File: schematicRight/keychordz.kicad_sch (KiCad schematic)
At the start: 41 parts, among them IC1 MCP73833-BZI_UN, J1 USB_C_Receptacle_USB2.0, J2 Conn_01x04_Male, J3 Conn_01x04_Male, SW1 SW_Push, SW2 SW_Push, SW3 SW_Push, SW4 SW_Push, SW5 SW_Push, SW6 SW_Push, SW7 SW_Push, SW9 SW_SPST, U1 nRF52840_Breakout

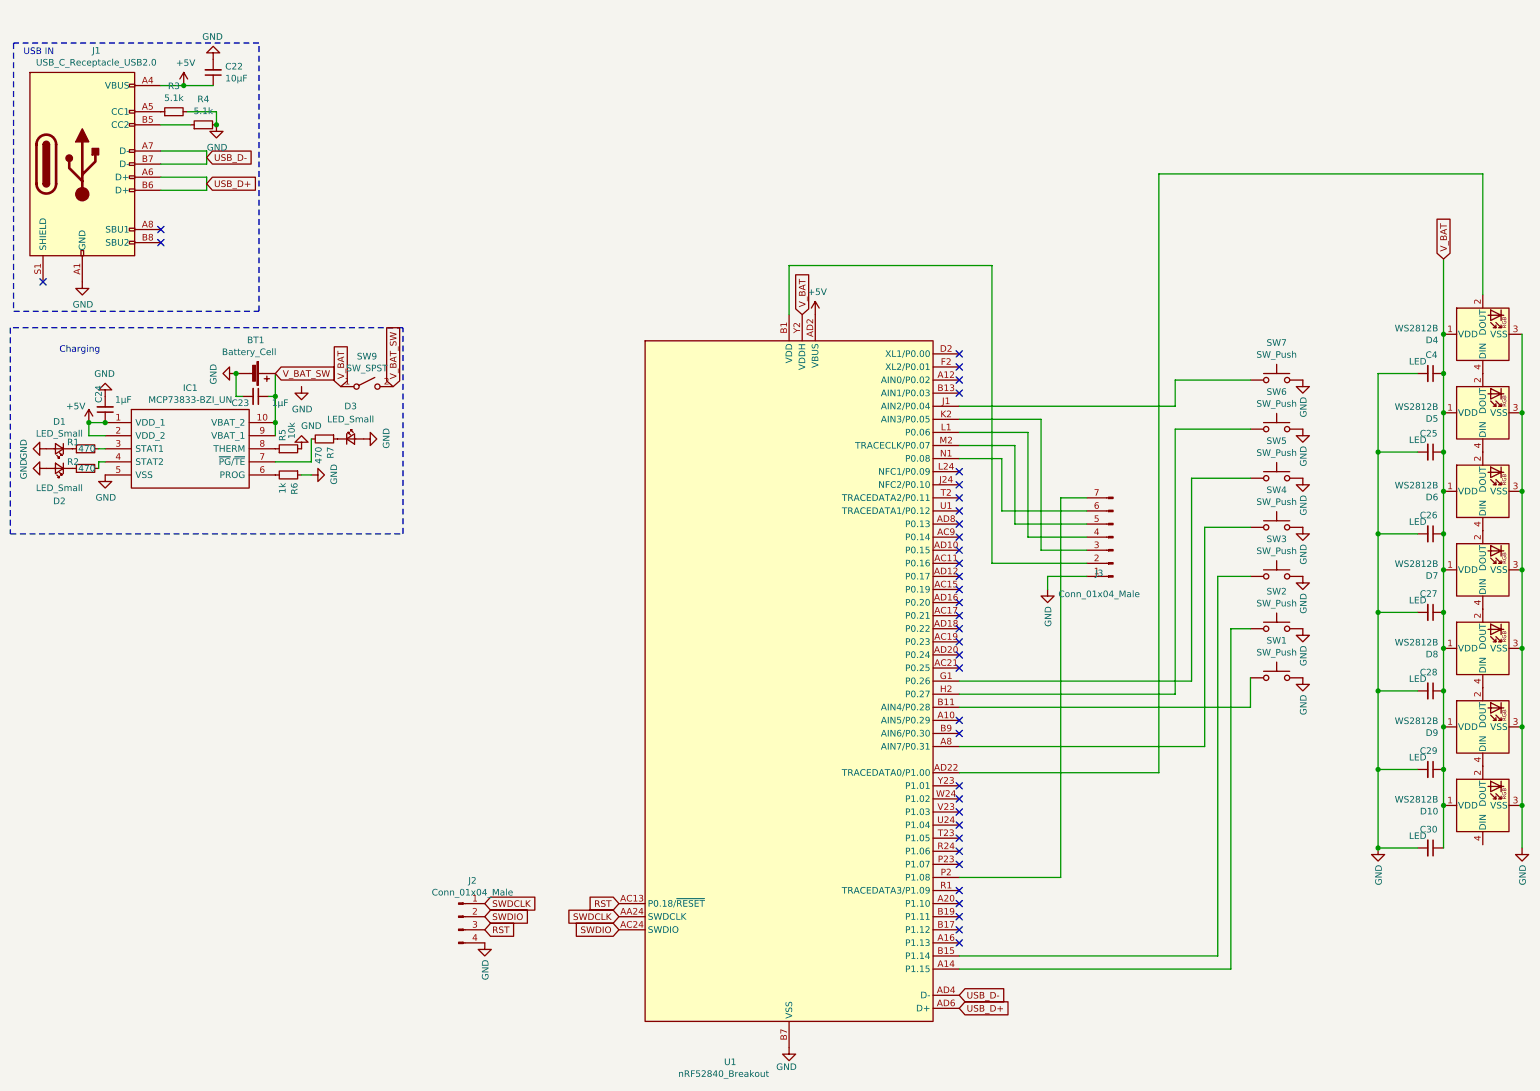
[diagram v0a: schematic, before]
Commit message: change right PCB to STM32
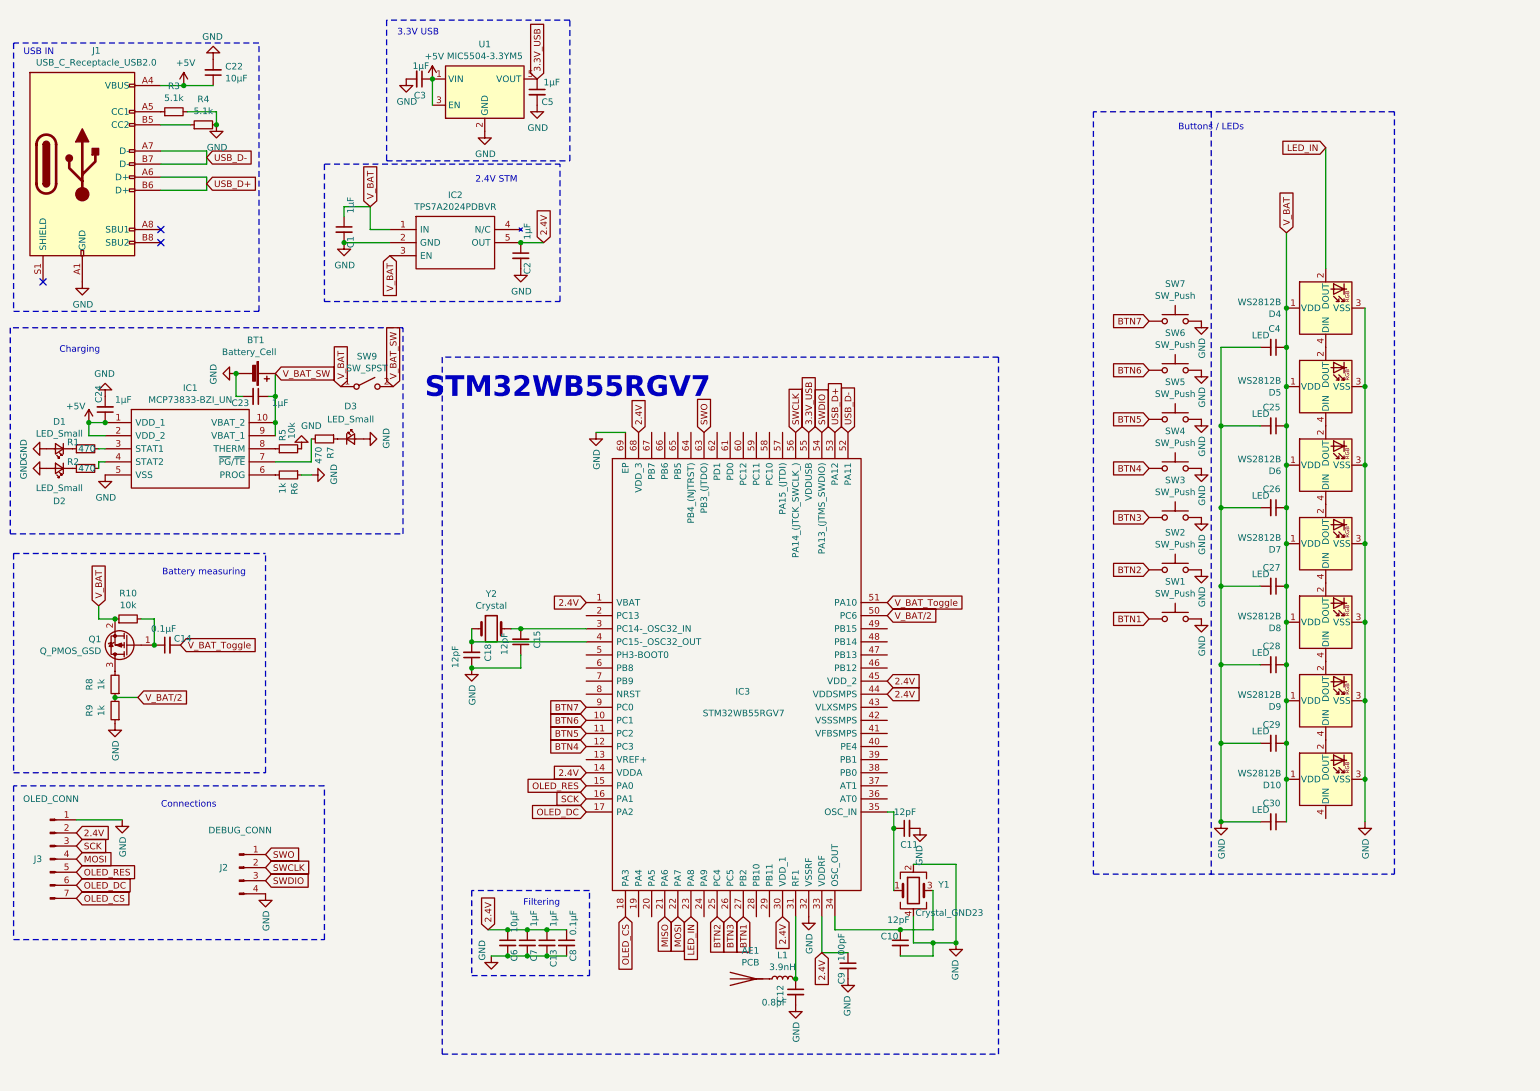
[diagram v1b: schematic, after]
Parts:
- removed U1: nRF52840_Breakout, schematic:nRF52840_Breakout, symbol MCU_Nordic:nRF52840_Breakout
- added AE1: PCB, RF_Antenna:Texas_SWRA117D_2.4GHz_Left, symbol Device:Antenna
- added C1, C13, C2, C3, C5, C7: 1µF, Capacitor_SMD:C_0402_1005Metric_Pad0.74x0.62mm_HandSolder, symbol Device:C_Small
- added C10, C11, C15, C18: 12pF, Capacitor_SMD:C_0603_1608Metric_Pad1.08x0.95mm_HandSolder, symbol Device:C_Small
- added C12: 0.8pF, Capacitor_SMD:C_0201_0603Metric_Pad0.64x0.40mm_HandSolder, symbol Device:C_Small
- added C14, C8: 0.1µF, Capacitor_SMD:C_0402_1005Metric_Pad0.74x0.62mm_HandSolder, symbol Device:C_Small
- added C6: 10µF, Capacitor_SMD:C_0402_1005Metric_Pad0.74x0.62mm_HandSolder, symbol Device:C_Small
- added C9: 100pF, Capacitor_SMD:C_0402_1005Metric_Pad0.74x0.62mm_HandSolder, symbol Device:C_Small
- added IC2: TPS7A2024PDBVR, SamacSys_Parts:SOT95P280X145-5N, symbol LoaderParts:TPS7A2033PDBVR
- added IC3: STM32WB55RGV7, SamacSys_Parts:QFN40P800X800X100-69N-D, symbol LoaderParts:STM32WB55RGV7
- added L1: 3.9nH, Inductor_SMD:L_0402_1005Metric_Pad0.77x0.64mm_HandSolder, symbol Device:L_Small
- added Q1: Q_PMOS_GSD, Package_TO_SOT_SMD:SC-59_Handsoldering, symbol Device:Q_PMOS_GSD
- added R10: 10k, Resistor_SMD:R_0603_1608Metric_Pad0.98x0.95mm_HandSolder, symbol Device:R_Small
- added R8, R9: 1k, Resistor_SMD:R_0603_1608Metric_Pad0.98x0.95mm_HandSolder, symbol Device:R_Small
- added U1: MIC5504-3.3YM5, Package_TO_SOT_SMD:SOT-23-5, symbol Regulator_Linear:MIC5504-3.3YM5
- added Y1: Crystal_GND23, Crystal:Crystal_SMD_2016-4Pin_2.0x1.6mm_HandSoldering, symbol Device:Crystal_GND24
- added Y2: Crystal, Crystal:Crystal_SMD_MicroCrystal_CC7V-T1A-2Pin_3.2x1.5mm_HandSoldering, symbol Device:Crystal
- J1: footprint Connector_USB:USB_C_Receptacle_Amphenol_12401548E4-2A -> SamacSys_Parts:SS52400002
- J2: value Conn_01x04_Male -> DEBUG_CONN
- J3: value Conn_01x04_Male -> OLED_CONN
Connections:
- net RST is gone; now on net SWDIO: J2.3 (Pin_3)
- net +5V: now also C3.1, U1.1 (VIN), U1.3 (EN)
- net GND: now also C1.2, C10.2, C11.2, C12.2, C13.2, C15.1, C18.1, C2.2, C3.2, C5.2, C6.2, C7.2, C8.2, C9.2, IC2.2 (GND), IC3.32 (VSSRF), IC3.69 (EP), R9.1, U1.2 (GND), Y1.2, Y1.4
- net SWDIO: now also IC3.54 (PA13_(JTMS_SWDIO)); no longer J2.2 (Pin_2)
- net USB_D+: now also IC3.53 (PA12)
- net USB_D-: now also IC3.52 (PA11)
- net V_BAT: now also C1.1, IC2.1 (IN), IC2.3 (EN), Q1.2 (S), R10.1
- net BTN5: now reaches SW5.1
- net BTN5: now also IC3.11 (PC2)
- net BTN4: now reaches SW4.1
- net BTN4: now also IC3.12 (PC3)
- net BTN3: now reaches SW3.1
- net BTN3: now also IC3.26 (PC5)
- net BTN2: now reaches SW2.1
- net BTN2: now also IC3.25 (PC4)
- net BTN1: now reaches SW1.1
- net BTN1: now also IC3.27 (PB2)
- net 2.4V: now reaches J3.2 (Pin_2)
- net 2.4V: now also C13.1, C2.1, C6.1, C7.1, C8.1, C9.1, IC2.5 (OUT), IC3.1 (VBAT), IC3.14 (VDDA), IC3.30 (VDD_1), IC3.33 (VDDRF), IC3.44 (VDDSMPS), IC3.45 (VDD_2), IC3.68 (VDD_3)
- net SCK: now reaches J3.3 (Pin_3)
- net SCK: now also IC3.16 (PA1)
- net MOSI: now reaches J3.4 (Pin_4)
- net MOSI: now also IC3.22 (PA7)
- net OLED_RES: now reaches J3.5 (Pin_5)
- net OLED_RES: now also IC3.15 (PA0)
- net OLED_DC: now reaches J3.6 (Pin_6)
- net OLED_DC: now also IC3.17 (PA2)
- net OLED_CS: now reaches J3.7 (Pin_7)
- net OLED_CS: now also IC3.18 (PA3)
- net BTN6: now reaches SW6.1
- net BTN6: now also IC3.10 (PC1)
- net LED_IN: now reaches D4.2 (DOUT)
- net LED_IN: now also IC3.23 (PA8)
- net BTN7: now reaches SW7.1
- net BTN7: now also IC3.9 (PC0)
- net SWDCLK renamed SWO
- net SWO: now also IC3.63 (PB3_(JTDO))
- new net: C12.1, IC3.31 (RF1), L1.2
- new net: C14.1, Q1.1 (G), R10.2
- new net: C15.2, IC3.3 (PC14-_OSC32_IN), Y2.2
- new net: C10.1, IC3.34 (OSC_OUT), Y1.3
- new net: C11.1, IC3.35 (OSC_IN), Y1.1
- new net: C18.2, IC3.4 (PC15-_OSC32_OUT), Y2.1
- new net: Q1.3 (D), R8.2
- new net: AE1.1 (A), L1.1
- new net 3.3V_USB: C5.1, IC3.55 (VDDUSB), U1.5 (VOUT)
- new net MISO: IC3.21 (PA6)
- new net SWCLK: IC3.56 (PA14_(JTCK_SWCLK_)), J2.2 (Pin_2)
- new net V_BAT_Toggle: C14.2, IC3.51 (PA10)
- new net V_BAT/2: IC3.50 (PC6), R8.1, R9.2
- no-connect marks 37 -> 3
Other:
- note added: "2.4V STM"
- note added: "3.3V USB"
- note added: "Battery measuring"
- note added: "Buttons / LEDs"
- note added: "Connections"
- note added: "Filtering"
- note added: "STM32WB55RGV7"
- moved on the sheet: C25, C26, C27, C28, C29, C30, C4, D10, D4, D5, D6, D7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

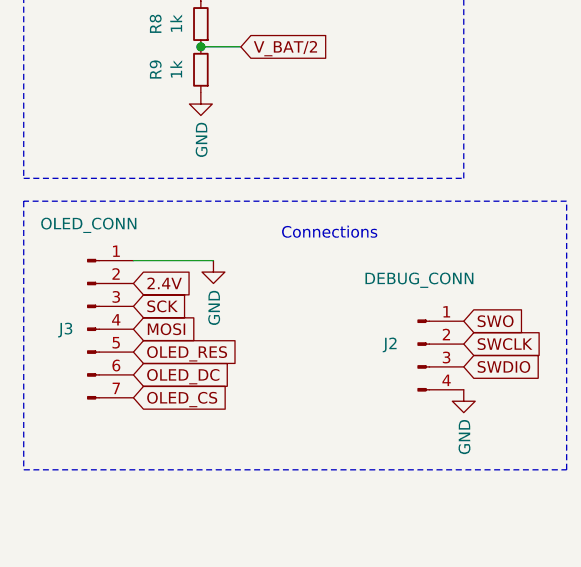
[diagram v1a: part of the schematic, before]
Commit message: change OLED voltage to V_BAT (ordered this commit)
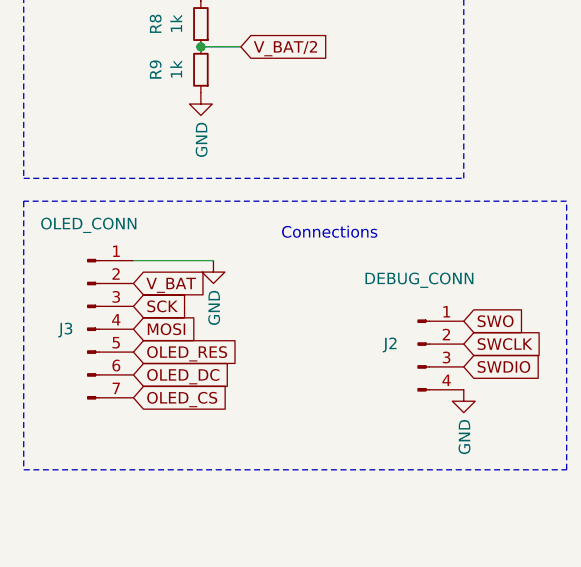
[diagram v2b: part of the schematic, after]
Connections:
- net 2.4V: no longer J3.2 (Pin_2)
- net V_BAT: now also J3.2 (Pin_2)
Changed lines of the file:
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@@
     (effects (font (size 1.27 1.27)) (justify right bottom))
   )
-  (global_label "2.4V" (shape input) (at 29.972 170.434 0)
+  (global_label "V_BAT" (shape input) (at 29.972 170.434 0)
     (effects (font (size 1.27 1.27)) (justify left))
-    (property "Intersheet References" "${INTERSHEET_REFS}" (id 0) (at 36.4975 170.5134 0)
+    (property "Intersheet References" "${INTERSHEET_REFS}" (id 0) (at 37.7675 170.3546 0)
       (effects (font (size 1.27 1.27)) (justify left) hide)
     )
